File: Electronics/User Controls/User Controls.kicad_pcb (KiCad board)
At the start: 2 copper layers, 29 parts, among them J1 TERM, J10 BUTTON 7, J11 BUTTON 8, J12 JOYSTICK 1, J13 JOYSTICK 2, J2 CAN BUS, J3 Conn_01x02, J4 BUTTON 1, J5 BUTTON 2, J6 BUTTON 3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

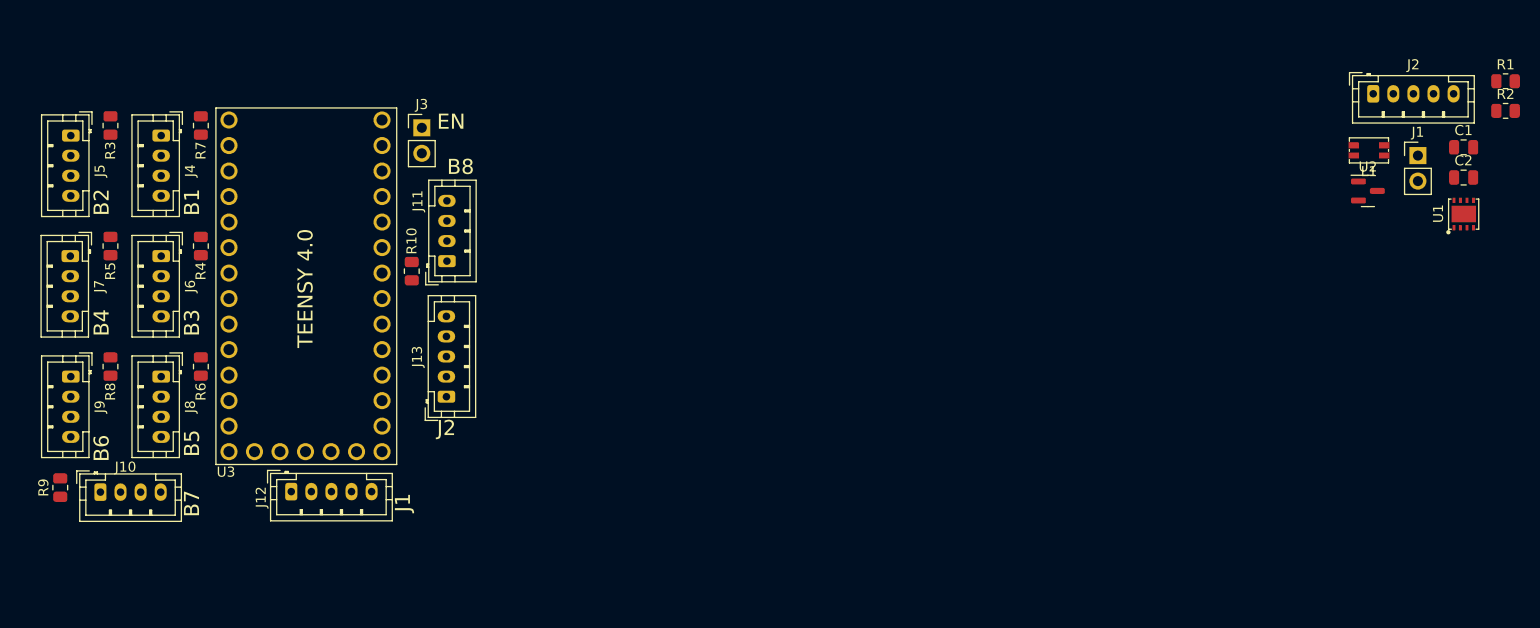
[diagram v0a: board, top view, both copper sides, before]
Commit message: Working on user controls PCB.
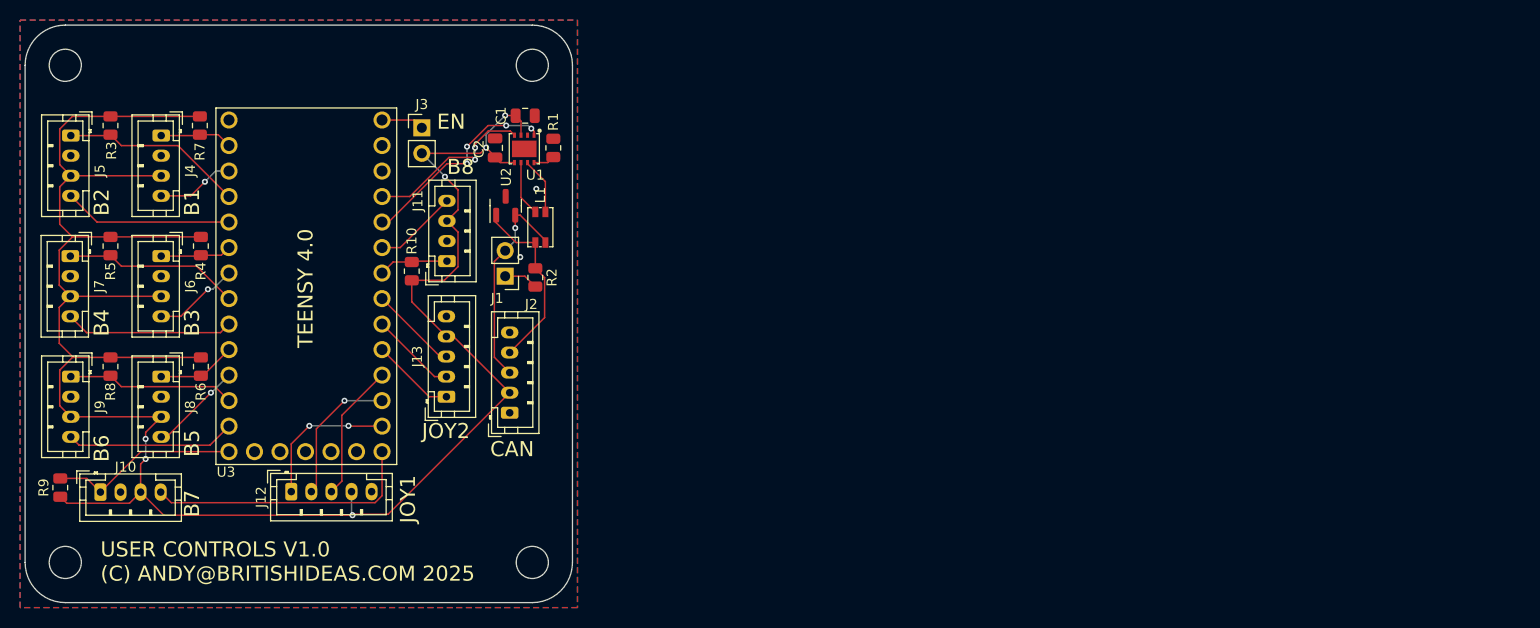
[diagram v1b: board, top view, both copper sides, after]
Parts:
- moved R2 98.0 mm to (149.8, 78.1), turned to -90 degrees
- moved C2 96.5 mm to (145.8, 65.2), turned to 90 degrees
- moved R1 95.1 mm to (151.6, 65.2), turned to -90 degrees
- moved C1 93.5 mm to (148.8, 62.0)
- moved U1 92.1 mm to (149.7, 64.0), turned to 180 degrees
- moved J1 91.7 mm to (146.8, 78.0), turned to 180 degrees
- moved J2 91.7 mm to (147.2, 91.6), turned to 90 degrees
- moved U2 85.9 mm to (146.8, 71.0), turned to 90 degrees
- moved L1 82.9 mm to (150.3, 73.1), turned to -90 degrees
- moved R7 0.10 mm to (116.4, 63.0)
- turned R3 to -90 degrees
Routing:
- net +5V: track 0.00 -> 214.2 mm, vias 0 -> 6
- net /B7_LED_GND: track 0.00 -> 27.2 mm
- net /CAN/CAN_H: track 0.00 -> 21.4 mm, vias 0 -> 1
- net /CAN/CAN_TX: track 0.00 -> 20.7 mm, vias 0 -> 4
- net /B7: track 0.00 -> 19.0 mm
- net /B2: track 0.00 -> 18.3 mm
- net /CAN/CAN_L: track 0.00 -> 18.2 mm
- net /B4: track 0.00 -> 17.6 mm
- net /CAN/CAN_RX: track 0.00 -> 17.1 mm, vias 0 -> 2
- net /B6_LED_GND: track 0.00 -> 16.9 mm
- net /B2_LED_GND: track 0.00 -> 16.8 mm
- net /B4_LED_GND: track 0.00 -> 16.8 mm
- net /B6: track 0.00 -> 16.8 mm
- net /J1_SW: track 0.00 -> 14.5 mm, vias 0 -> 2
- net /J1_Y: track 0.00 -> 14.2 mm, vias 0 -> 1
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- added copper zone on B.Cu, net GND
- added copper zone on F.Cu, net GND
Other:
- board outline added: 54.5 x 57.5 mm
- board text added: "CAN"
- board text added: "JOY1"
- board text added: "JOY2"
- board text added: "USER CONTROLS V1.0 (C) ANDY@BRITISHIDEAS.COM 2025"
- board text removed: "J1"
- board text removed: "J2"

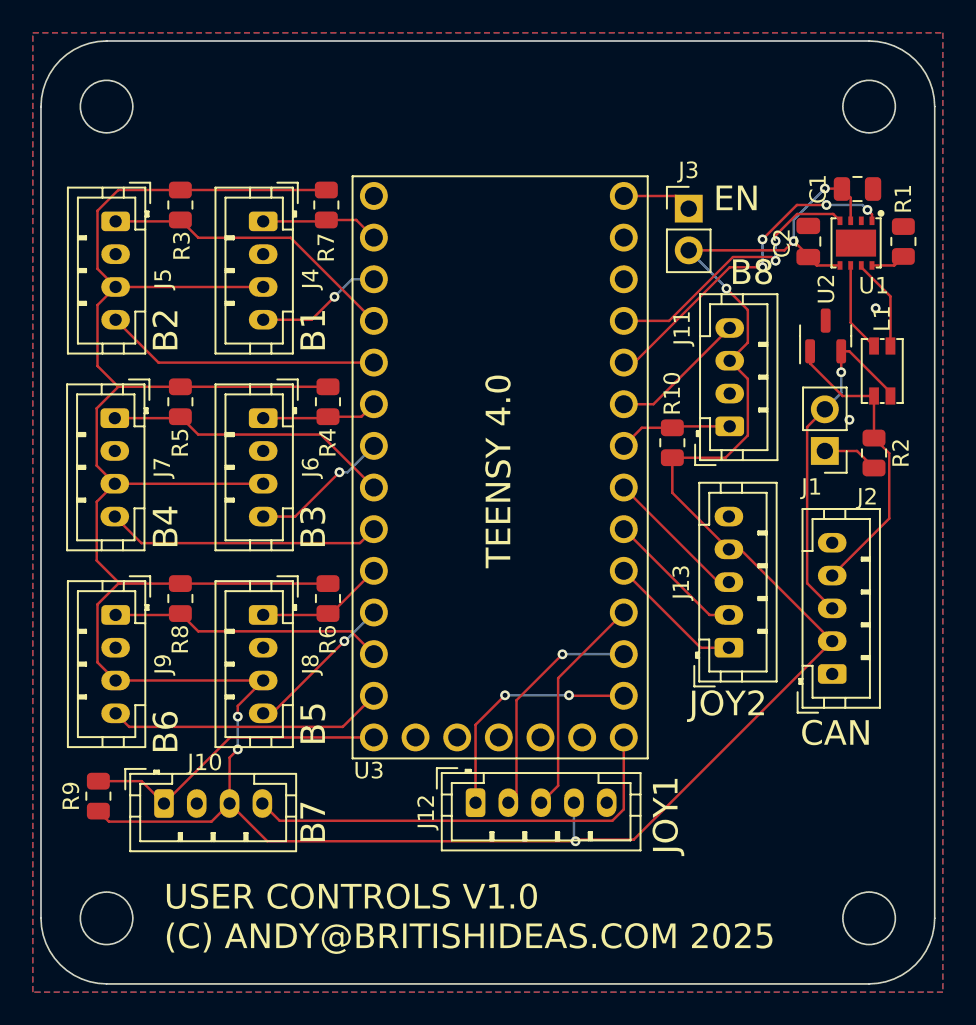
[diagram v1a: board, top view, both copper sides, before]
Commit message: Finished first attempt at user controls PCB.
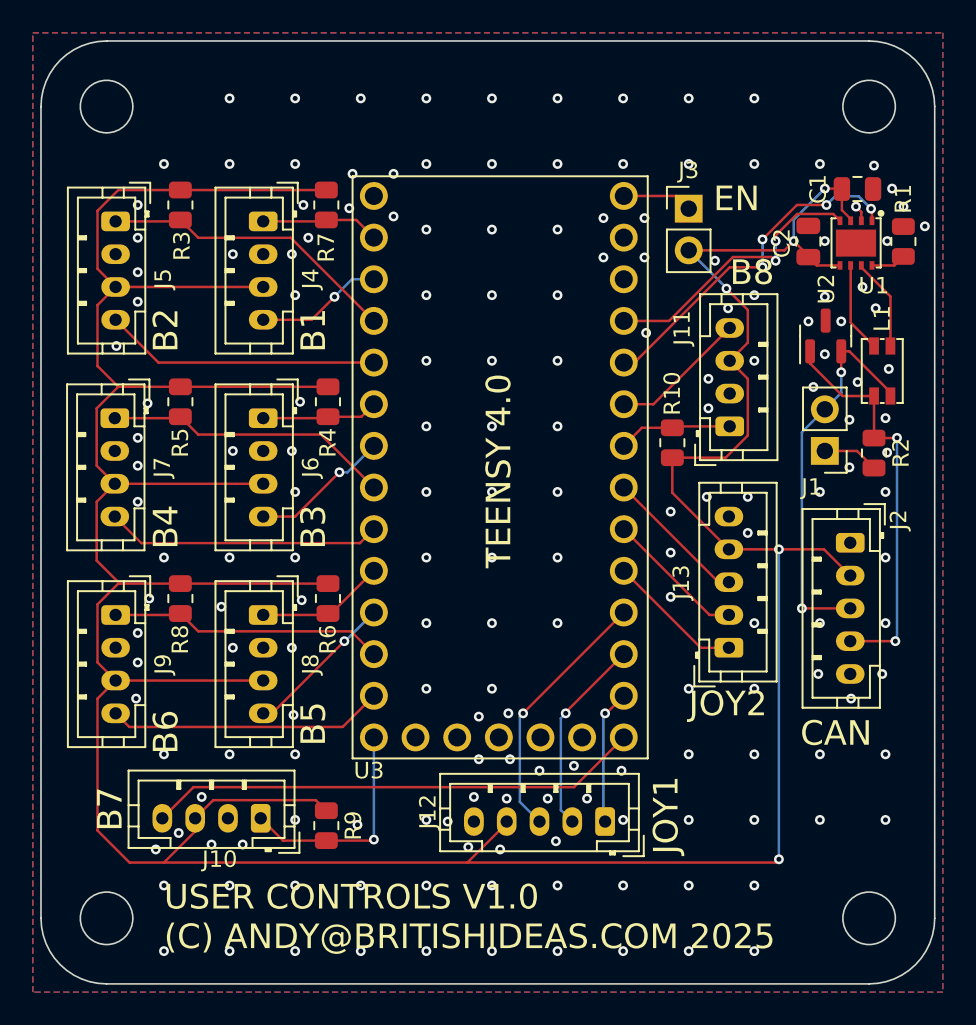
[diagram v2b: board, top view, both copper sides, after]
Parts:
- moved R9 14.0 mm to (116.4, 100.8), turned to -90 degrees
- moved J2 8.08 mm to (148.3, 83.6), turned to -90 degrees
- moved J12 7.98 mm to (133.4, 100.6), turned to 180 degrees
- moved J10 5.97 mm to (112.4, 100.4), turned to 180 degrees
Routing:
- net +5V: track 214.2 -> 238.1 mm, vias 6 -> 5
- net /CAN/CAN_L: track 18.2 -> 24.6 mm, vias 0 -> 2
- net /J1_SW: track 14.5 -> 8.37 mm, vias 2 -> 1
- net /B7: track 19.0 -> 13.7 mm, vias 0 -> 1
- net /B7_LED_GND: track 27.2 -> 30.2 mm
- net /CAN/CAN_H: track 21.4 -> 23.9 mm, vias 1 -> 2
- net /J1_X: track 13.7 -> 15.9 mm, vias 0 -> 1
- net /J1_Y: track 14.2 -> 12.9 mm
- net GND: track 0.00 -> 1.00 mm, vias 2 -> 179
- net /CAN/CAN_TX: track 20.7 -> 21.3 mm

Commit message: Added fiducials to all boards.
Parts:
- added FID1: Fiducial, Fiducial:Fiducial_0.5mm_Mask1mm, F.Cu at (108.2, 56.2)
- added FID2: Fiducial, Fiducial:Fiducial_0.5mm_Mask1mm, F.Cu at (144.6, 56.2)
- added FID3: Fiducial, Fiducial:Fiducial_0.5mm_Mask1mm, F.Cu at (145.8, 102.2)
